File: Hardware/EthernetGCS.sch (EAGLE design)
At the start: 63 parts, among them IC3 24AA00OT, IC4 PIC24FJ64GA002_QFN, J2 HR911105A, Q2 25Mhz, U1 MIC5219-3.3V, U4 ENC28J60-QFN, U5 MIC5219-3.3V, U7 FT232RL-BASICSSOP, X2 USB-A-H

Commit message: Cleaning the schematic
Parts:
- removed C17: 10uF, rcl:CPOL-EUSMCA
- removed R10: 49R9 1%, SparkFun:RESISTOR0402-RES
- added C4: 0.1uF, SparkFun:CAP0402-CAP
- added C5: 1uF, SparkFun:CAP0402-CAP
- added R12: 49R9 1%, SparkFun:RESISTOR0402-RES
- added U3: MIC5219-3.3V, SparkFun:V_REG_LDOSMD
- C15: value 0.1uF -> 470pF
- C16: value 0.1uF -> 10uF; device rcl:C-EUC0805 -> SparkFun:CAP_POL1206
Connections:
- net N$10 renamed LED_TX
- net N$11 renamed LED_RX
- net SCL_1 renamed SCL
- net SDA_1 renamed SDA
- removed net ETH-INT: U4.INT
- removed net ETH-RST: U4.RESET
- new net N$3: C15.1, U3.BP
- net 3.3V: now also C16.+, U3.OUT
- net 5V: now also C5.1, U3.EN, U3.IN
- net CCT: now also C14.2, R12.1, R9.1; no longer C15.1, R10.2, R9.2
- net GND: now also C16.-, C4.2, C5.2, U3.GND; no longer C16.2, C17.-
- net N$22: now also C4.1, R7.1, R8.1; no longer C14.2, R7.2, R8.2
- net RD+: now also R7.2; no longer R8.1
- net RD-: now also R8.2; no longer R7.1
- net TD+: now also R12.2; no longer R10.1
- net TD-: now also R9.2; no longer R9.1
- net V+: no longer C16.1, C17.+
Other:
- note added: "Ethernet MAC and PHY"
- note added: "MAC Address"
- note added: "MISC"
- note added: "Power RF"
- note added: "Power uC"
- note added: "RF Transceiver"
- note added: "uC"
- note removed: "R12"
- note removed: "Version B1,4 = 2.7K ohm"
- note removed: "Version B5,7 = 2.32K ohm"
- moved on the sheet: C1, C10, C11, C12, C13, C14, C15, C18, C19, C2, C20, C3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

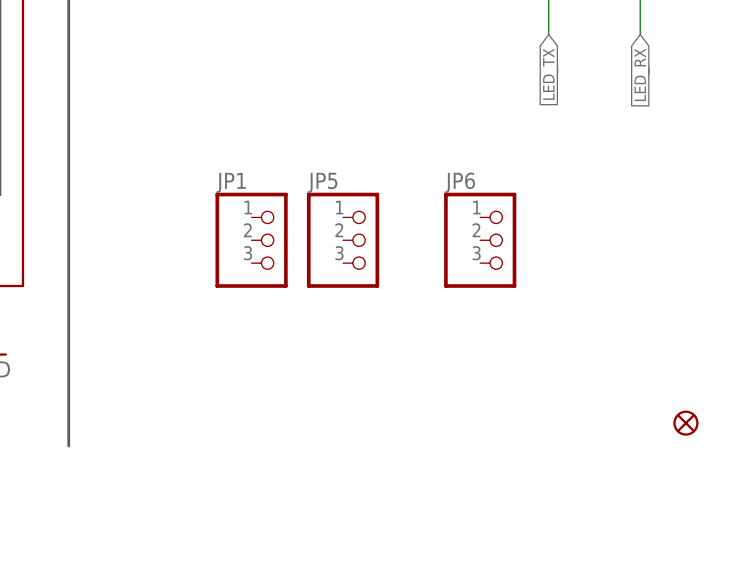
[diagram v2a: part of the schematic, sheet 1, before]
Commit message: Changing the RC connectors for the one in the SparkFun library
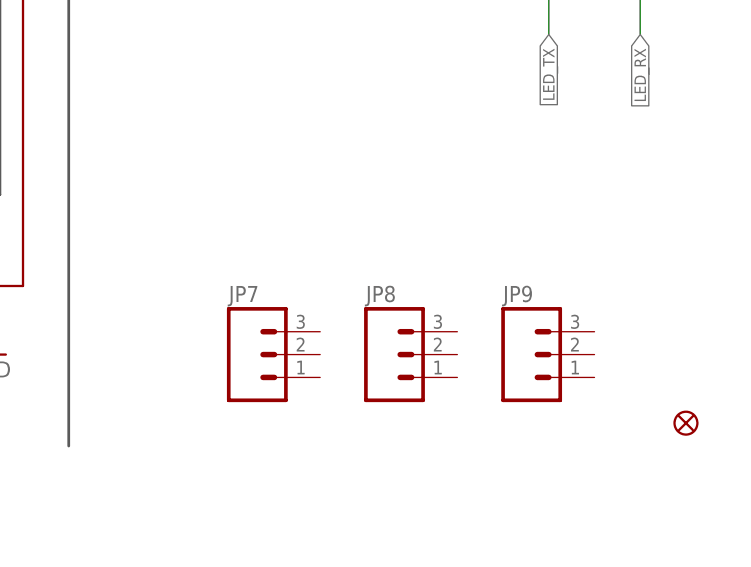
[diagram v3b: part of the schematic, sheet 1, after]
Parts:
- removed JP1, JP5, JP6: (no value), pinhead:PINHD-1X3
- added JP7, JP8, JP9: (no value), SparkFun-Connectors:M03PTH
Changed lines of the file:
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@@
 <part name="L3" library="pel_dipol_comp" deviceset="INDUCTOR" device="-0402" value="BLM15HD102SN1"/>
 <part name="L7" library="pel_dipol_comp" deviceset="INDUCTOR" device="-0402" value="BKP1005HS121-T"/>
-<part name="JP1" library="pinhead" deviceset="PINHD-1X3" device=""/>
-<part name="JP5" library="pinhead" deviceset="PINHD-1X3" device=""/>
-<part name="JP6" library="pinhead" deviceset="PINHD-1X3" device=""/>
 <part name="R12" library="SparkFun" deviceset="RESISTOR" device="0402-RES" value="49R9 1%"/>
 <part name="C4" library="SparkFun" deviceset="CAP" device="0402-CAP" value="0.1uF"/>
@@
 <part name="U$2" library="SparkFun" deviceset="5V" device=""/>
 <part name="P+4" library="SparkFun" deviceset="3.3V" device=""/>
+<part name="JP7" library="SparkFun-Connectors" deviceset="M03" device="PTH"/>
+<part name="JP8" library="SparkFun-Connectors" deviceset="M03" device="PTH"/>
+<part name="JP9" library="SparkFun-Connectors" deviceset="M03" device="PTH"/>
 </parts>
 <sheets>
@@
 <instance part="C19" gate="G$1" x="68.58" y="55.88"/>
 <instance part="C20" gate="G$1" x="73.66" y="55.88"/>
-<instance part="JP1" gate="A" x="198.12" y="58.42"/>
-<instance part="JP5" gate="A" x="208.28" y="58.42"/>
-<instance part="JP6" gate="A" x="223.52" y="58.42"/>
 <instance part="R12" gate="G$1" x="121.92" y="96.52" smashed="yes" rot="R90">
 <attribute name="NAME" x="125.5014" y="92.71" size="1.778" layer="95" rot="R90"/>
@@
 <instance part="U$2" gate="G$1" x="76.2" y="170.18"/>
 <instance part="P+4" gate="G$1" x="129.54" y="170.18"/>
+<instance part="JP7" gate="G$1" x="195.58" y="45.72"/>
+<instance part="JP8" gate="G$1" x="210.82" y="45.72"/>
+<instance part="JP9" gate="G$1" x="226.06" y="45.72"/>
 </instances>
 <busses>

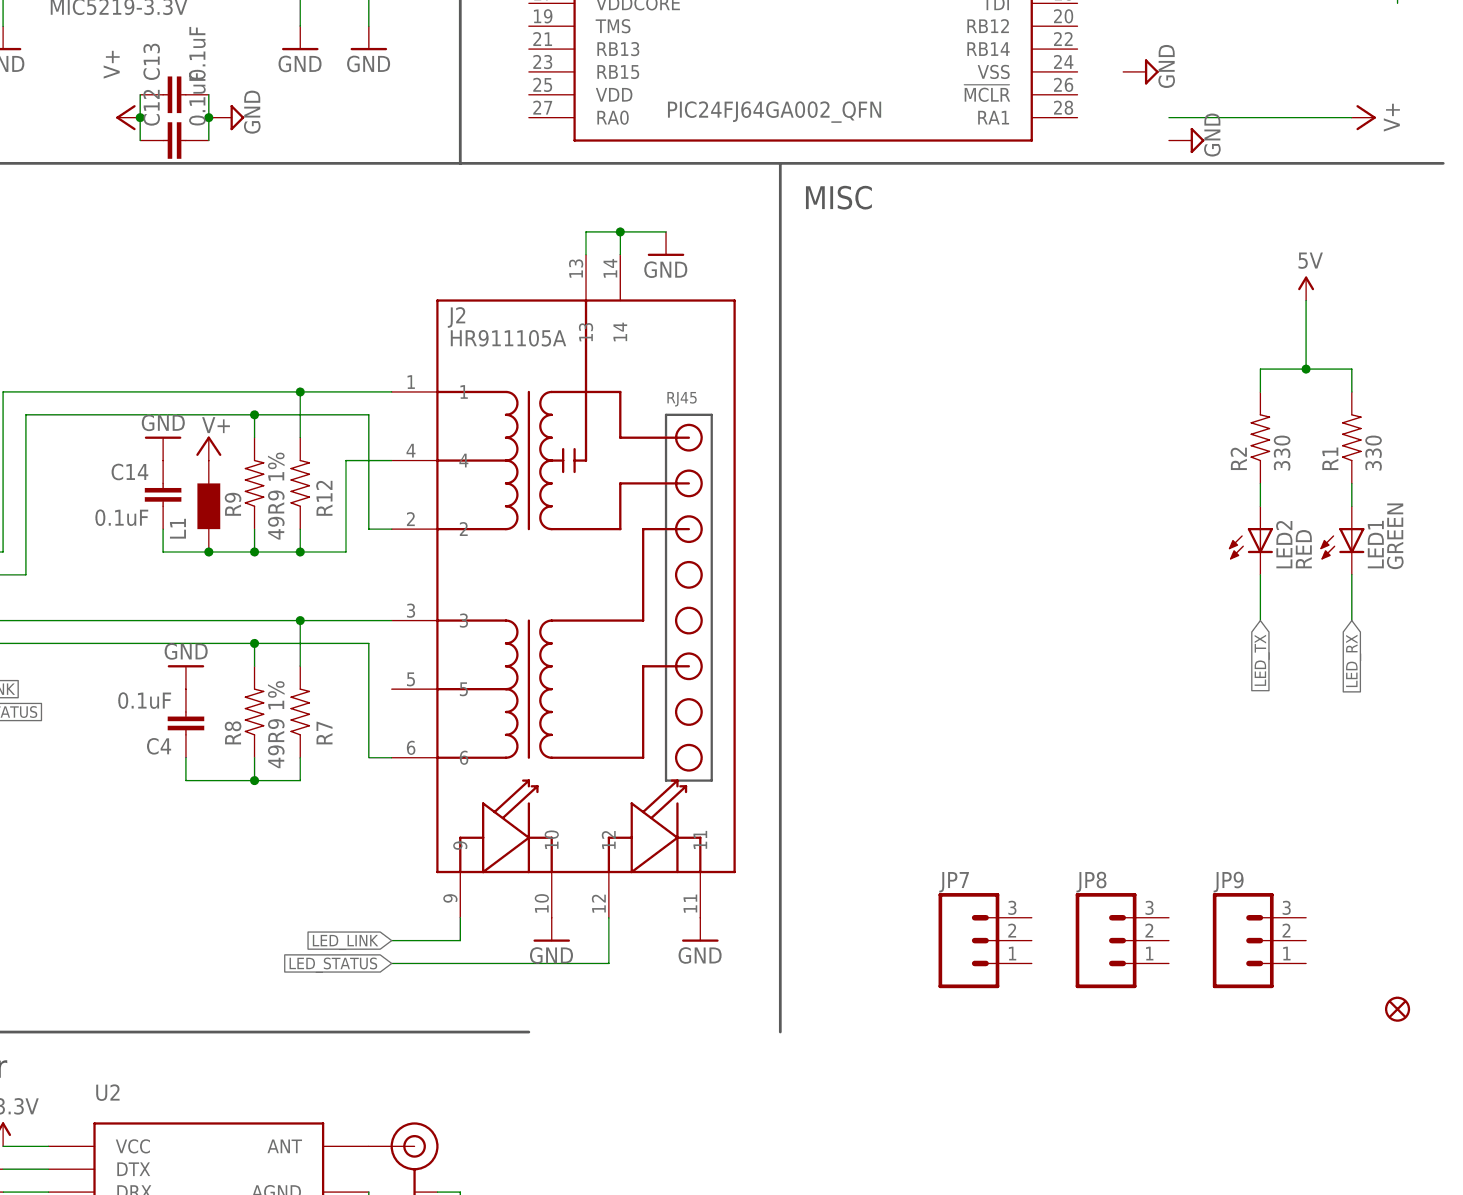
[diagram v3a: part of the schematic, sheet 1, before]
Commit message: Adding information to the RC section
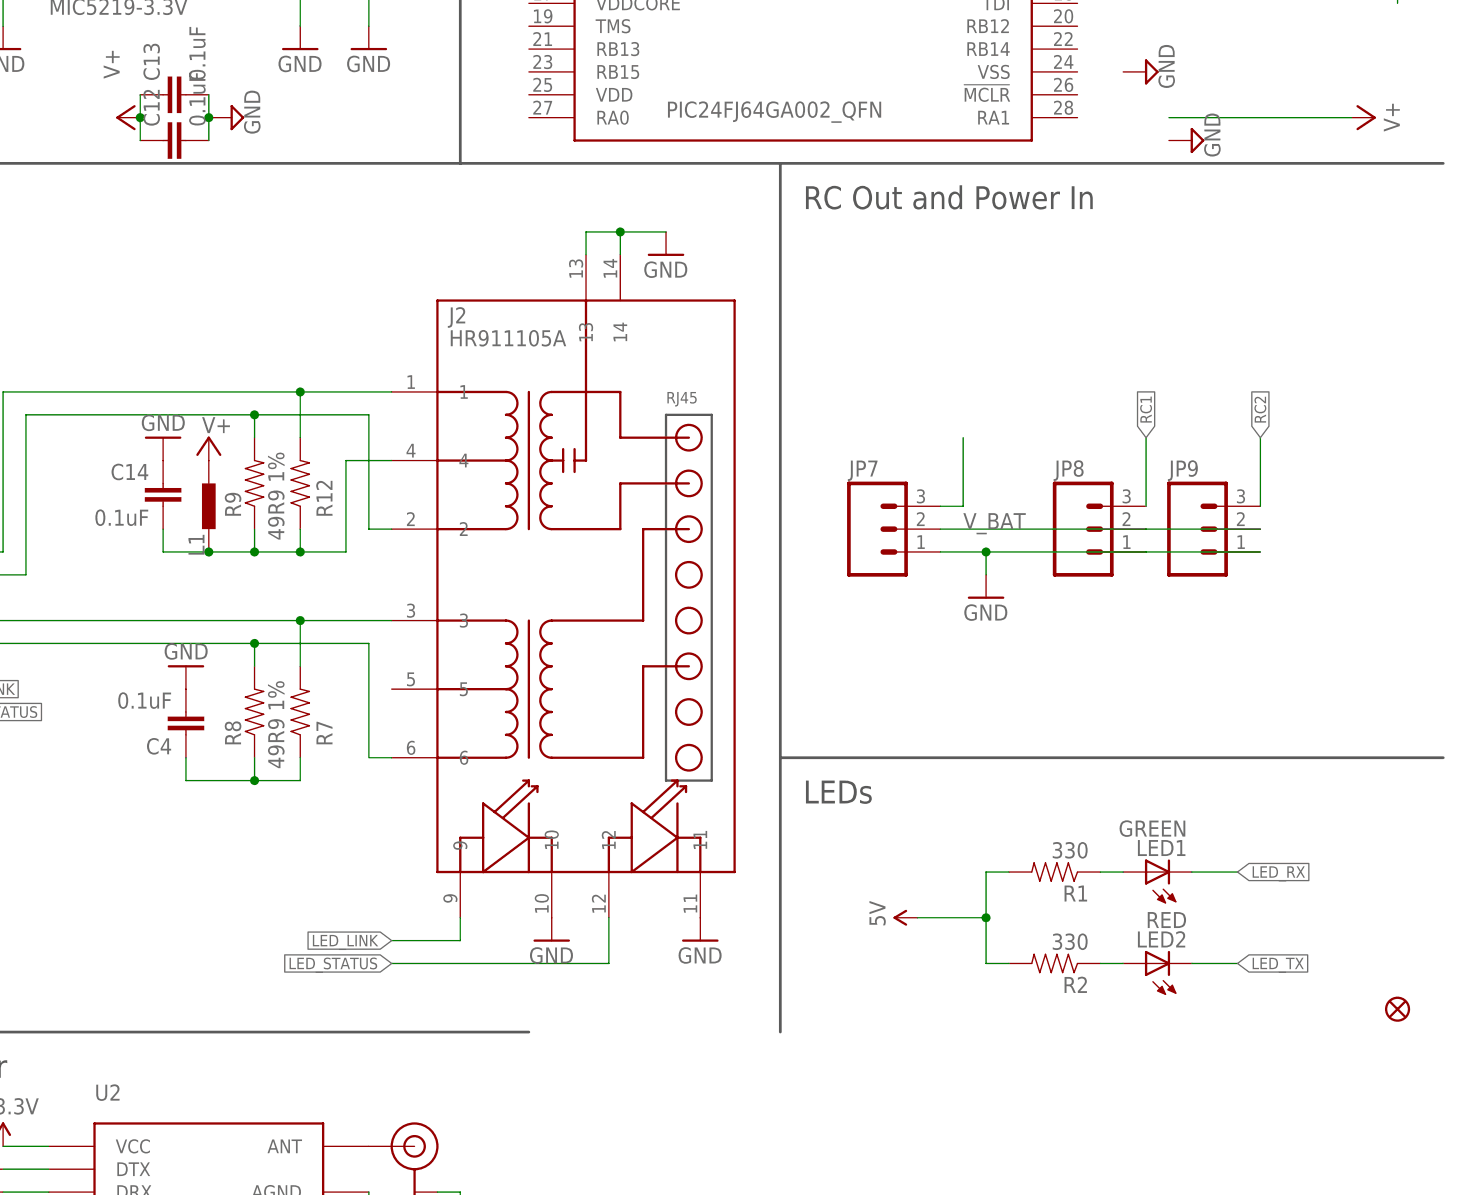
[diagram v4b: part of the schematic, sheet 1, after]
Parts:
- L1: value (none) -> BLM15HD102SN1; device wuerth-elektronik:WE-KIL_0805 -> pel_dipol_comp:INDUCTOR-0402
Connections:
- new net BAT_MON: JP7.3
- new net RC1: JP8.3
- new net RC2: JP9.3
- new net V_BAT: JP7.2, JP8.2, JP9.2
- net GND: now also JP7.1, JP8.1, JP9.1
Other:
- note added: "LEDs"
- note added: "RC Out and Power In"
- note removed: "MISC"
- moved on the sheet: JP7, JP8, JP9, L1, LED1, LED2, R1, R2
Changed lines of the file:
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@@
 <part name="GND12" library="supply1" deviceset="GND" device=""/>
 <part name="GND13" library="supply1" deviceset="GND" device=""/>
-<part name="L1" library="wuerth-elektronik" deviceset="WE-KIL" device="_0805"/>
 <part name="V14" library="supply2" deviceset="GND" device=""/>
 <part name="P+8" library="supply2" deviceset="V+" device=""/>
@@
 <part name="JP8" library="SparkFun-Connectors" deviceset="M03" device="PTH"/>
 <part name="JP9" library="SparkFun-Connectors" deviceset="M03" device="PTH"/>
+<part name="L1" library="pel_dipol_comp" deviceset="INDUCTOR" device="-0402" value="BLM15HD102SN1"/>
+<part name="GND28" library="supply1" deviceset="GND" device=""/>
 </parts>
 <sheets>
@@
 <text x="2.54" y="30.48" size="2.54" layer="97">MAC Address</text>
 <text x="66.04" y="30.48" size="2.54" layer="97">RF Transceiver</text>
-<wire x1="175.26" y1="132.08" x2="175.26" y2="35.56" width="0.3048" layer="97"/>
+<wire x1="175.26" y1="132.08" x2="175.26" y2="66.04" width="0.3048" layer="97"/>
 <text x="2.54" y="127" size="2.54" layer="97">Ethernet MAC and PHY</text>
-<text x="177.8" y="127" size="2.54" layer="97">MISC</text>
+<text x="177.8" y="127" size="2.54" layer="97">RC Out and Power In</text>
+<text x="177.8" y="60.96" size="2.54" layer="97">LEDs</text>
+<wire x1="175.26" y1="66.04" x2="175.26" y2="35.56" width="0.3048" layer="97"/>
+<wire x1="175.26" y1="66.04" x2="248.92" y2="66.04" width="0.3048" layer="97"/>
 </plain>
 <instances>
@@
 <instance part="GND7" gate="1" x="139.7" y="5.08"/>
 <instance part="JP2" gate="G$1" x="243.84" y="38.1"/>
-<instance part="LED1" gate="G$1" x="238.76" y="91.44"/>
-<instance part="LED2" gate="G$1" x="228.6" y="91.44"/>
-<instance part="R1" gate="G$1" x="238.76" y="101.6" rot="R90"/>
-<instance part="R2" gate="G$1" x="228.6" y="101.6" rot="R90"/>
-<instance part="U$4" gate="G$1" x="233.68" y="116.84"/>
+<instance part="LED1" gate="G$1" x="215.9" y="53.34" rot="R90"/>
+<instance part="LED2" gate="G$1" x="215.9" y="43.18" rot="R90"/>
+<instance part="R1" gate="G$1" x="205.74" y="53.34" rot="R180"/>
+<instance part="R2" gate="G$1" x="205.74" y="43.18" rot="R180"/>
+<instance part="U$4" gate="G$1" x="190.5" y="48.26" rot="R90"/>
 <instance part="L4" gate="G$1" x="83.82" y="20.32" smashed="yes" rot="R90">
 <attribute name="NAME" x="78.232" y="20.8026" size="1.778" layer="95"/>
@@
 <instance part="GND12" gate="1" x="109.22" y="76.2" rot="R180"/>
 <instance part="GND13" gate="1" x="106.68" y="101.6" rot="R180"/>
-<instance part="L1" gate="G$1" x="111.76" y="93.98" rot="R90"/>
 <instance part="V14" gate="GND" x="17.78" y="48.26"/>
 <instance part="P+8" gate="1" x="111.76" y="101.6" smashed="yes">
@@
 <instance part="U$2" gate="G$1" x="76.2" y="170.18"/>
 <instance part="P+4" gate="G$1" x="129.54" y="170.18"/>
-<instance part="JP7" gate="G$1" x="195.58" y="45.72"/>
-<instance part="JP8" gate="G$1" x="210.82" y="45.72"/>
-<instance part="JP9" gate="G$1" x="226.06" y="45.72"/>
+<instance part="JP7" gate="G$1" x="185.42" y="91.44"/>
+<instance part="JP8" gate="G$1" x="208.28" y="91.44"/>
+<instance part="JP9" gate="G$1" x="220.98" y="91.44"/>
+<instance part="L1" gate="G$1" x="111.76" y="93.98" smashed="yes" rot="R180">
+<attribute name="NAME" x="111.2774" y="88.392" size="1.778" layer="95" rot="R90"/>
+</instance>
+<instance part="GND28" gate="1" x="198.12" y="83.82"/>
 </instances>
 <busses>
@@
 <pinref part="GND27" gate="1" pin="GND"/>
 </segment>
+<segment>
+<pinref part="JP7" gate="G$1" pin="1"/>
+<pinref part="JP8" gate="G$1" pin="1"/>
+<wire x1="193.04" y1="88.9" x2="198.12" y2="88.9" width="0.1524" layer="91"/>
+<pinref part="JP9" gate="G$1" pin="1"/>
+<wire x1="198.12" y1="88.9" x2="215.9" y2="88.9" width="0.1524" layer="91"/>
+<wire x1="215.9" y1="88.9" x2="228.6" y2="88.9" width="0.1524" layer="91"/>
+<pinref part="GND28" gate="1" pin="GND"/>
+<wire x1="198.12" y1="86.36" x2="198.12" y2="88.9" width="0.1524" layer="91"/>
+<junction x="198.12" y="88.9"/>
+</segment>
 </net>
 <net name="N$2" class="0">
@@
 </segment>
 <segment>
-<wire x1="228.6" y1="106.68" x2="228.6" y2="109.22" width="0.1524" layer="91"/>
-<wire x1="228.6" y1="109.22" x2="233.68" y2="109.22" width="0.1524" layer="91"/>
-<wire x1="233.68" y1="109.22" x2="233.68" y2="116.84" width="0.1524" layer="91"/>
-<wire x1="238.76" y1="106.68" x2="238.76" y2="109.22" width="0.1524" layer="91"/>
-<wire x1="238.76" y1="109.22" x2="233.68" y2="109.22" width="0.1524" layer="91"/>
-<junction x="233.68" y="109.22"/>
+<wire x1="200.66" y1="43.18" x2="198.12" y2="43.18" width="0.1524" layer="91"/>
+<wire x1="198.12" y1="43.18" x2="198.12" y2="48.26" width="0.1524" layer="91"/>
+<wire x1="198.12" y1="48.26" x2="190.5" y2="48.26" width="0.1524" layer="91"/>
+<wire x1="200.66" y1="53.34" x2="198.12" y2="53.34" width="0.1524" layer="91"/>
+<wire x1="198.12" y1="53.34" x2="198.12" y2="48.26" width="0.1524" layer="91"/>
+<junction x="198.12" y="48.26"/>
 <pinref part="R2" gate="G$1" pin="2"/>
 <pinref part="R1" gate="G$1" pin="2"/>
@@
 <net name="N$8" class="0">
 <segment>
-<wire x1="228.6" y1="96.52" x2="228.6" y2="93.98" width="0.1524" layer="91"/>
+<wire x1="210.82" y1="43.18" x2="213.36" y2="43.18" width="0.1524" layer="91"/>
 <pinref part="R2" gate="G$1" pin="1"/>
 <pinref part="LED2" gate="G$1" pin="A"/>
@@
 <net name="N$9" class="0">
 <segment>
-<wire x1="238.76" y1="96.52" x2="238.76" y2="93.98" width="0.1524" layer="91"/>
+<wire x1="210.82" y1="53.34" x2="213.36" y2="53.34" width="0.1524" layer="91"/>
 <pinref part="R1" gate="G$1" pin="1"/>
 <pinref part="LED1" gate="G$1" pin="A"/>
@@
 <net name="LED_TX" class="0">
 <segment>
-<wire x1="228.6" y1="86.36" x2="228.6" y2="81.28" width="0.1524" layer="91"/>
+<wire x1="220.98" y1="43.18" x2="226.06" y2="43.18" width="0.1524" layer="91"/>
 <pinref part="LED2" gate="G$1" pin="C"/>
-<label x="228.6" y="81.28" size="1.27" layer="95" rot="R270" xref="yes"/>
+<label x="226.06" y="43.18" size="1.27" layer="95" xref="yes"/>
 <wire x1="210.82" y1="154.94" x2="215.9" y2="154.94" width="0.1524" layer="91"/>
 <label x="215.9" y="154.94" size="1.27" layer="95" xref="yes"/>
@@
 <net name="LED_RX" class="0">
 <segment>
-<wire x1="238.76" y1="86.36" x2="238.76" y2="81.28" width="0.1524" layer="91"/>
+<wire x1="220.98" y1="53.34" x2="226.06" y2="53.34" width="0.1524" layer="91"/>
 <pinref part="LED1" gate="G$1" pin="C"/>
-<label x="238.76" y="81.28" size="1.27" layer="95" rot="R270" xref="yes"/>
+<label x="226.06" y="53.34" size="1.27" layer="95" xref="yes"/>
 <wire x1="210.82" y1="152.4" x2="215.9" y2="152.4" width="0.1524" layer="91"/>
 <label x="215.9" y="152.4" size="1.27" layer="95" xref="yes"/>
@@
 </segment>
 <segment>
-<pinref part="L1" gate="G$1" pin="2"/>
-<pinref part="P+8" gate="1" pin="V+"/>
-</segment>
-<segment>
 <wire x1="40.64" y1="20.32" x2="53.34" y2="20.32" width="0.1524" layer="91"/>
 <wire x1="53.34" y1="20.32" x2="53.34" y2="17.78" width="0.1524" layer="91"/>
@@
 <pinref part="IC3" gate="G$1" pin="VCC"/>
 <pinref part="C18" gate="G$1" pin="1"/>
+</segment>
+<segment>
+<pinref part="P+8" gate="1" pin="V+"/>
+<pinref part="L1" gate="G$1" pin="2"/>
 </segment>
 </net>
@@
 <net name="CCT" class="0">
 <segment>
-<pinref part="L1" gate="G$1" pin="1"/>
 <wire x1="127" y1="88.9" x2="127" y2="99.06" width="0.1524" layer="91"/>
 <pinref part="R12" gate="G$1" pin="1"/>
@@
 <wire x1="127" y1="88.9" x2="121.92" y2="88.9" width="0.1524" layer="91"/>
 <wire x1="121.92" y1="88.9" x2="116.84" y2="88.9" width="0.1524" layer="91"/>
-<wire x1="116.84" y1="88.9" x2="111.76" y2="88.9" width="0.1524" layer="91"/>
 <wire x1="116.84" y1="91.44" x2="116.84" y2="88.9" width="0.1524" layer="91"/>
 <wire x1="121.92" y1="91.44" x2="121.92" y2="88.9" width="0.1524" layer="91"/>
@@
 <pinref part="C14" gate="G$1" pin="2"/>
 <pinref part="R9" gate="G$1" pin="1"/>
-<junction x="111.76" y="88.9"/>
 <junction x="116.84" y="88.9"/>
 <junction x="121.92" y="88.9"/>
+<pinref part="L1" gate="G$1" pin="1"/>
+<wire x1="111.76" y1="88.9" x2="116.84" y2="88.9" width="0.1524" layer="91"/>
+<junction x="111.76" y="88.9"/>
 </segment>
 </net>
@@
 </segment>
 </net>
+<net name="V_BAT" class="0">
+<segment>
+<pinref part="JP7" gate="G$1" pin="2"/>
+<pinref part="JP8" gate="G$1" pin="2"/>
+<wire x1="193.04" y1="91.44" x2="215.9" y2="91.44" width="0.1524" layer="91"/>
+<pinref part="JP9" gate="G$1" pin="2"/>
+<wire x1="215.9" y1="91.44" x2="228.6" y2="91.44" width="0.1524" layer="91"/>
+<label x="195.58" y="91.44" size="1.778" layer="95"/>
+</segment>
+</net>
+<net name="BAT_MON" class="0">
+<segment>
+<pinref part="JP7" gate="G$1" pin="3"/>
+<wire x1="193.04" y1="93.98" x2="195.58" y2="93.98" width="0.1524" layer="91"/>
+<wire x1="195.58" y1="93.98" x2="195.58" y2="101.6" width="0.1524" layer="91"/>
+</segment>
+</net>
+<net name="RC1" class="0">
+<segment>
+<pinref part="JP8" gate="G$1" pin="3"/>
+<wire x1="215.9" y1="93.98" x2="215.9" y2="101.6" width="0.1524" layer="91"/>
+<label x="215.9" y="101.6" size="1.27" layer="95" rot="R90" xref="yes"/>
+</segment>
+</net>
+<net name="RC2" class="0">
+<segment>
+<pinref part="JP9" gate="G$1" pin="3"/>
+<wire x1="228.6" y1="93.98" x2="228.6" y2="101.6" width="0.1524" layer="91"/>
+<label x="228.6" y="101.6" size="1.27" layer="95" rot="R90" xref="yes"/>
+</segment>
+</net>
